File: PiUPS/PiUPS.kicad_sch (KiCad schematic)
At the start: 111 parts, among them J1 USB_C_Receptacle_USB2.0, J2 USB_B_Micro, J3 Screw_Terminal_01x02, J4 Raspberry_Pi_2_3, J5 USB_A, Q1 IRF7404, Q2 IRF7404, Q3 IRLML2803TRPBF, Q4 IRF7404, Q5 IRF7404, Q6 IRLML2803TRPBF, Q7 IRLML2803TRPBF, Q8 IRF7404, Q9 IRLML2803TRPBF, SW1 SW_MEC_5E, SW2 MODE (JS102011SAQN), U1 LM393, U2 BQ25895RTW, U3 DW01, U4 FS8205A, U5 TPS61088RHLR, U6 DS3231M

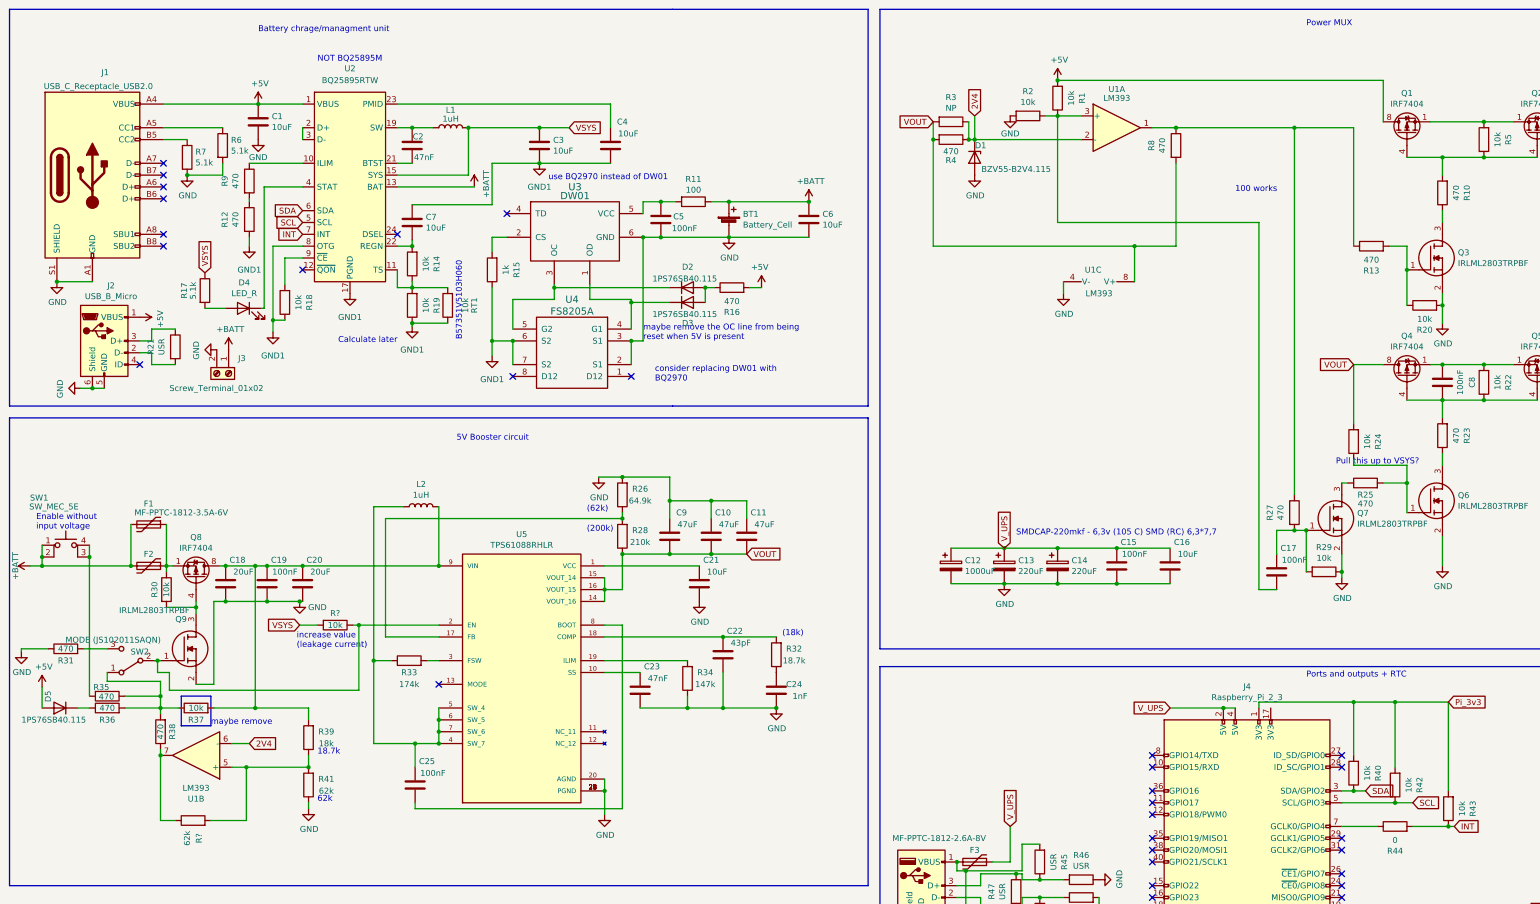
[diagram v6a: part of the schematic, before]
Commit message: updated components and schematic sligtly
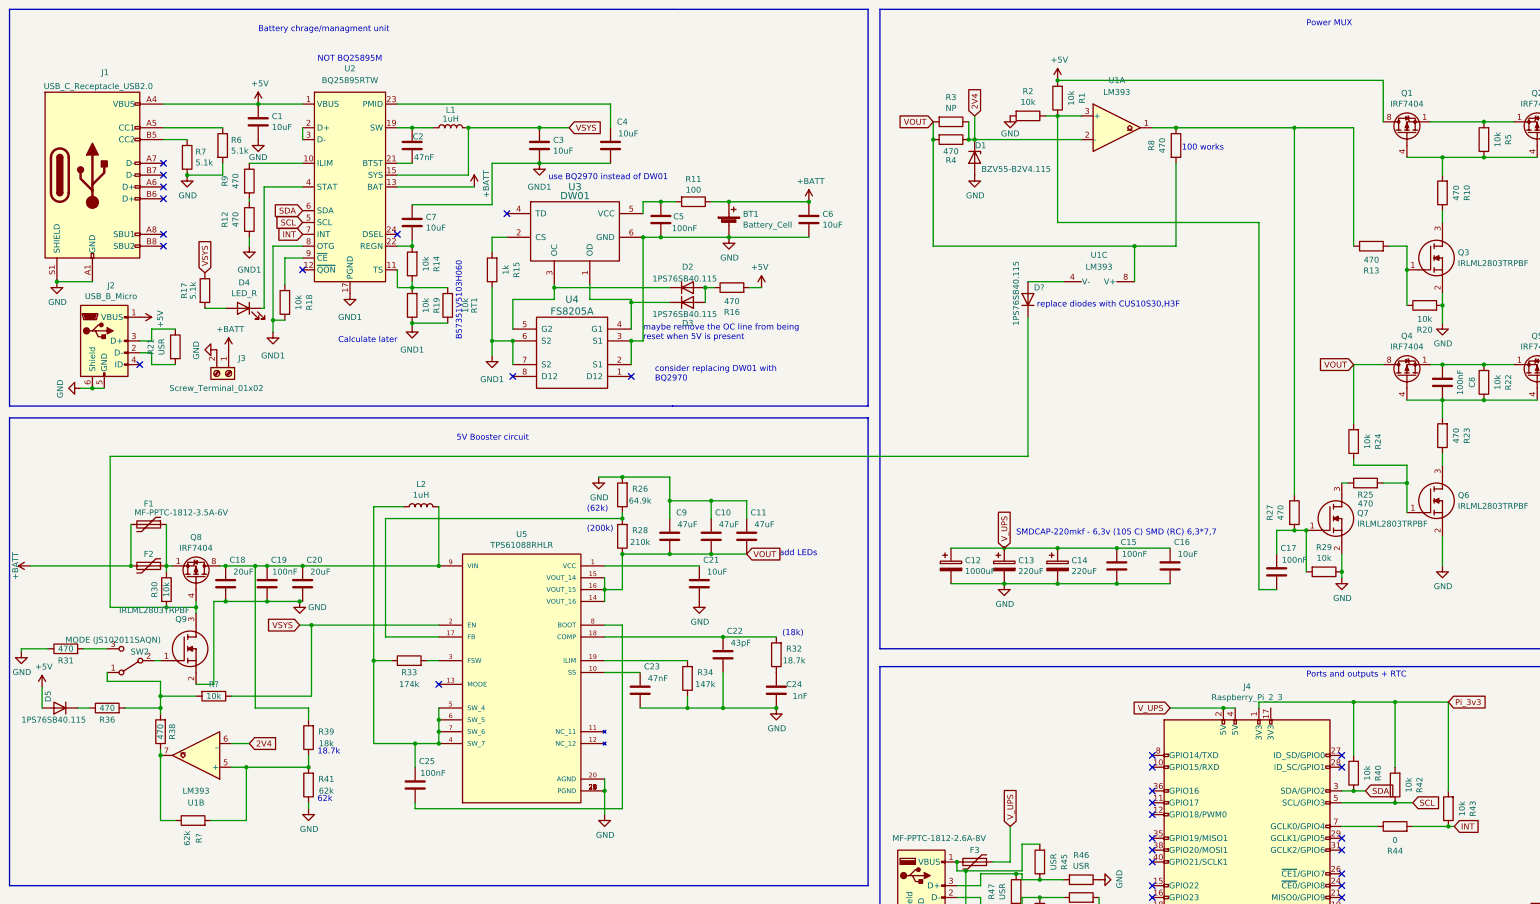
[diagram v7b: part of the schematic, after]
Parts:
- removed R35: 470, Resistor_SMD:R_0805_2012Metric_Pad1.20x1.40mm_HandSolder, symbol Device:R
- removed R37: 10k, Resistor_SMD:R_0805_2012Metric_Pad1.20x1.40mm_HandSolder, symbol Device:R
- removed SW1: SW_MEC_5E, Button_Switch_SMD:SW_SPST_Omron_B3FS-100xP, symbol Switch:SW_MEC_5E
- removed U1: LM393, Package_SO:SOIC-8_3.9x4.9mm_P1.27mm, symbol Amplifier_Operational:LM358
- added D?: 1PS76SB40.115, Diode_SMD:D_SOD-323_HandSoldering, symbol Diode:1N4007
- added U1: LM393, symbol Comparator:LM393
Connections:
- net 2V4: now also U1.2 (-), U1.6 (_)
- net VOUT: now also U1.8 (V+)
- net VSYS: now also R?.1, U5.2 (EN); no longer R?.2
- net at Q9.1, SW2.2 (B): no longer R?.1, U5.2 (EN)
- net at R13.1, R27.1, R8.1: now also U1.1
- net at R36.2, R38.2, SW2.1 (A): now also R?.2
- net at C17.2, R1.1, R2.1: now also U1.3 (+)
- net at R39.1, R41.2, R?.2: now also U1.5 (+)
- net at R38.1, R?.1: now also U1.7
- net at Q8.4 (G), Q9.3, R30.2: now also D?.1 (K)
- new net: D?.2 (A), U1.4 (V-)
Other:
- note added: "add LEDs"
- note added: "replace diodes with CUS10S30,H3F"
- note removed: "Enable without input voltage"
- note removed: "Pull this up to VSYS?"
- note removed: "increase value (leakage current)"
- note removed: "maybe remove"
- moved on the sheet: R?

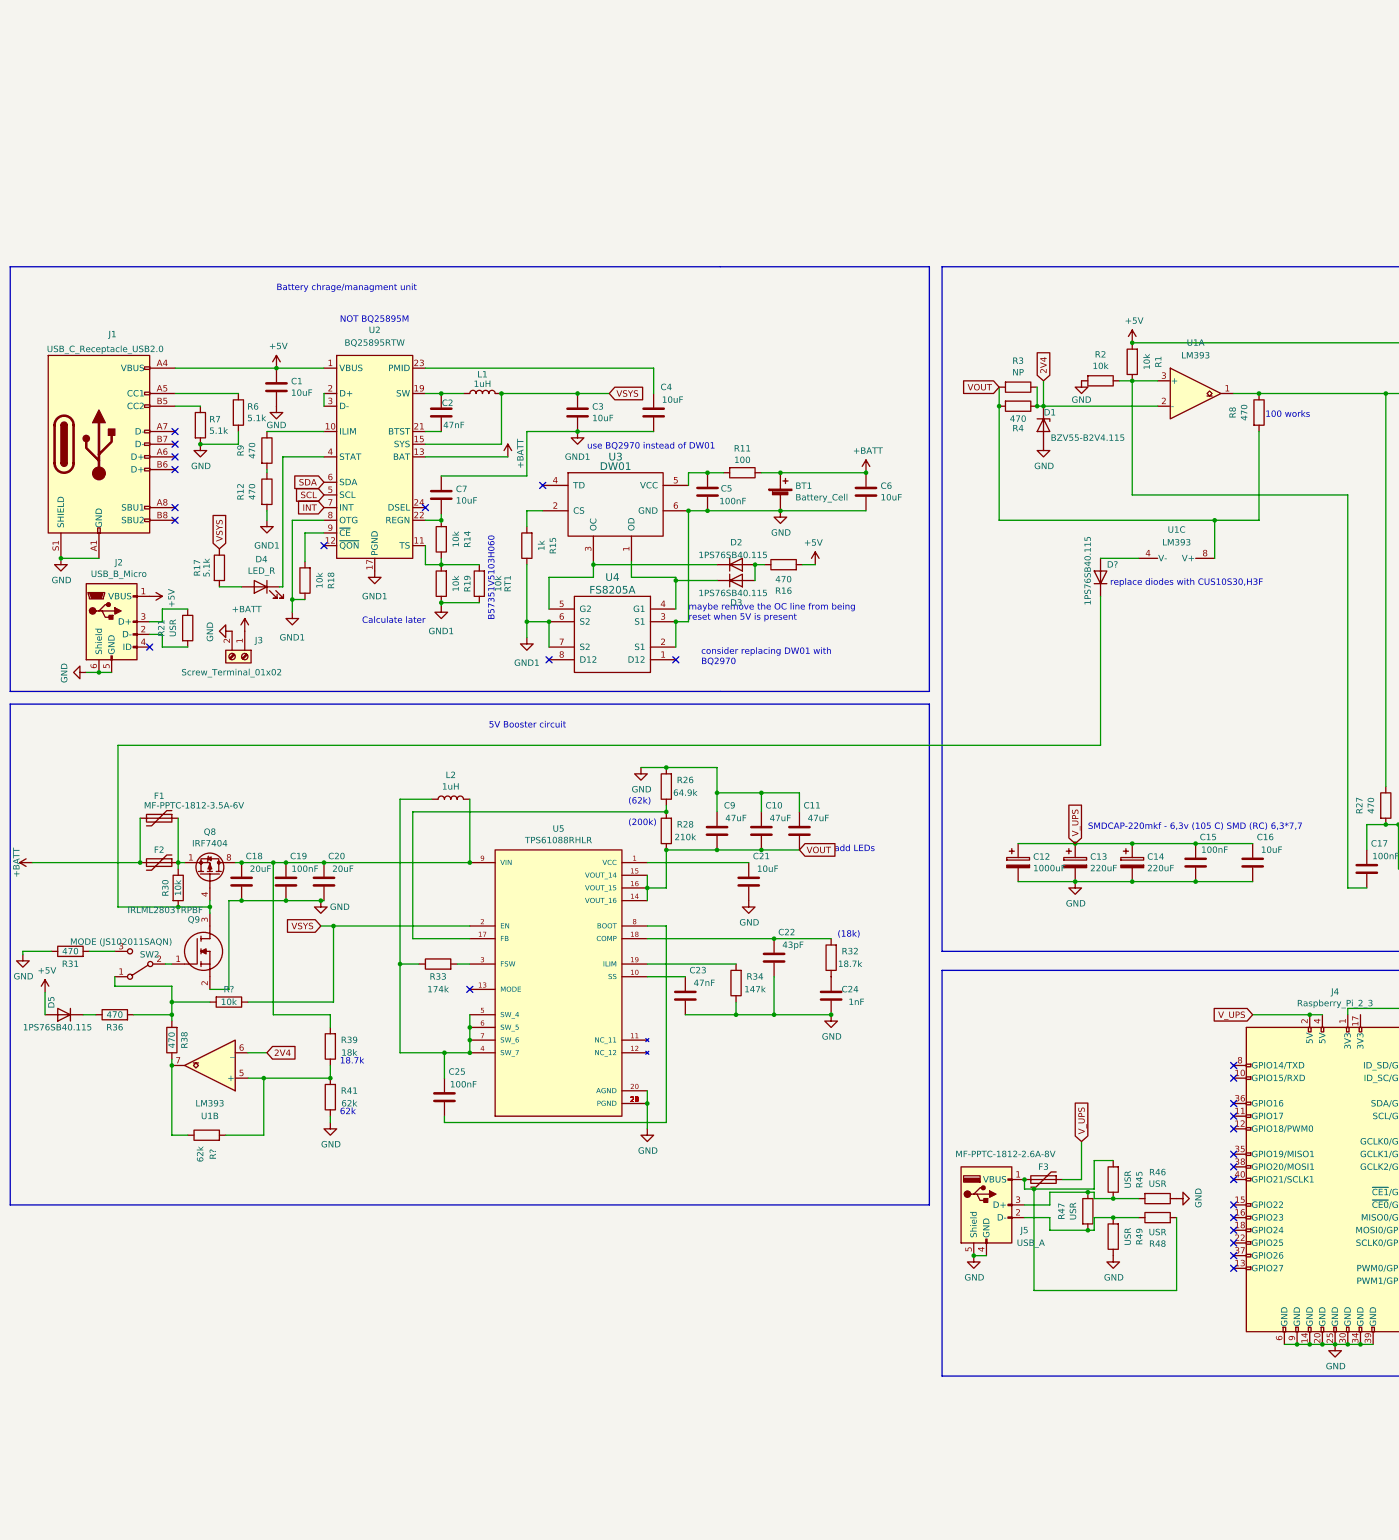
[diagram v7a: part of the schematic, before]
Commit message: updated shcematic with new battery protection system and some notes
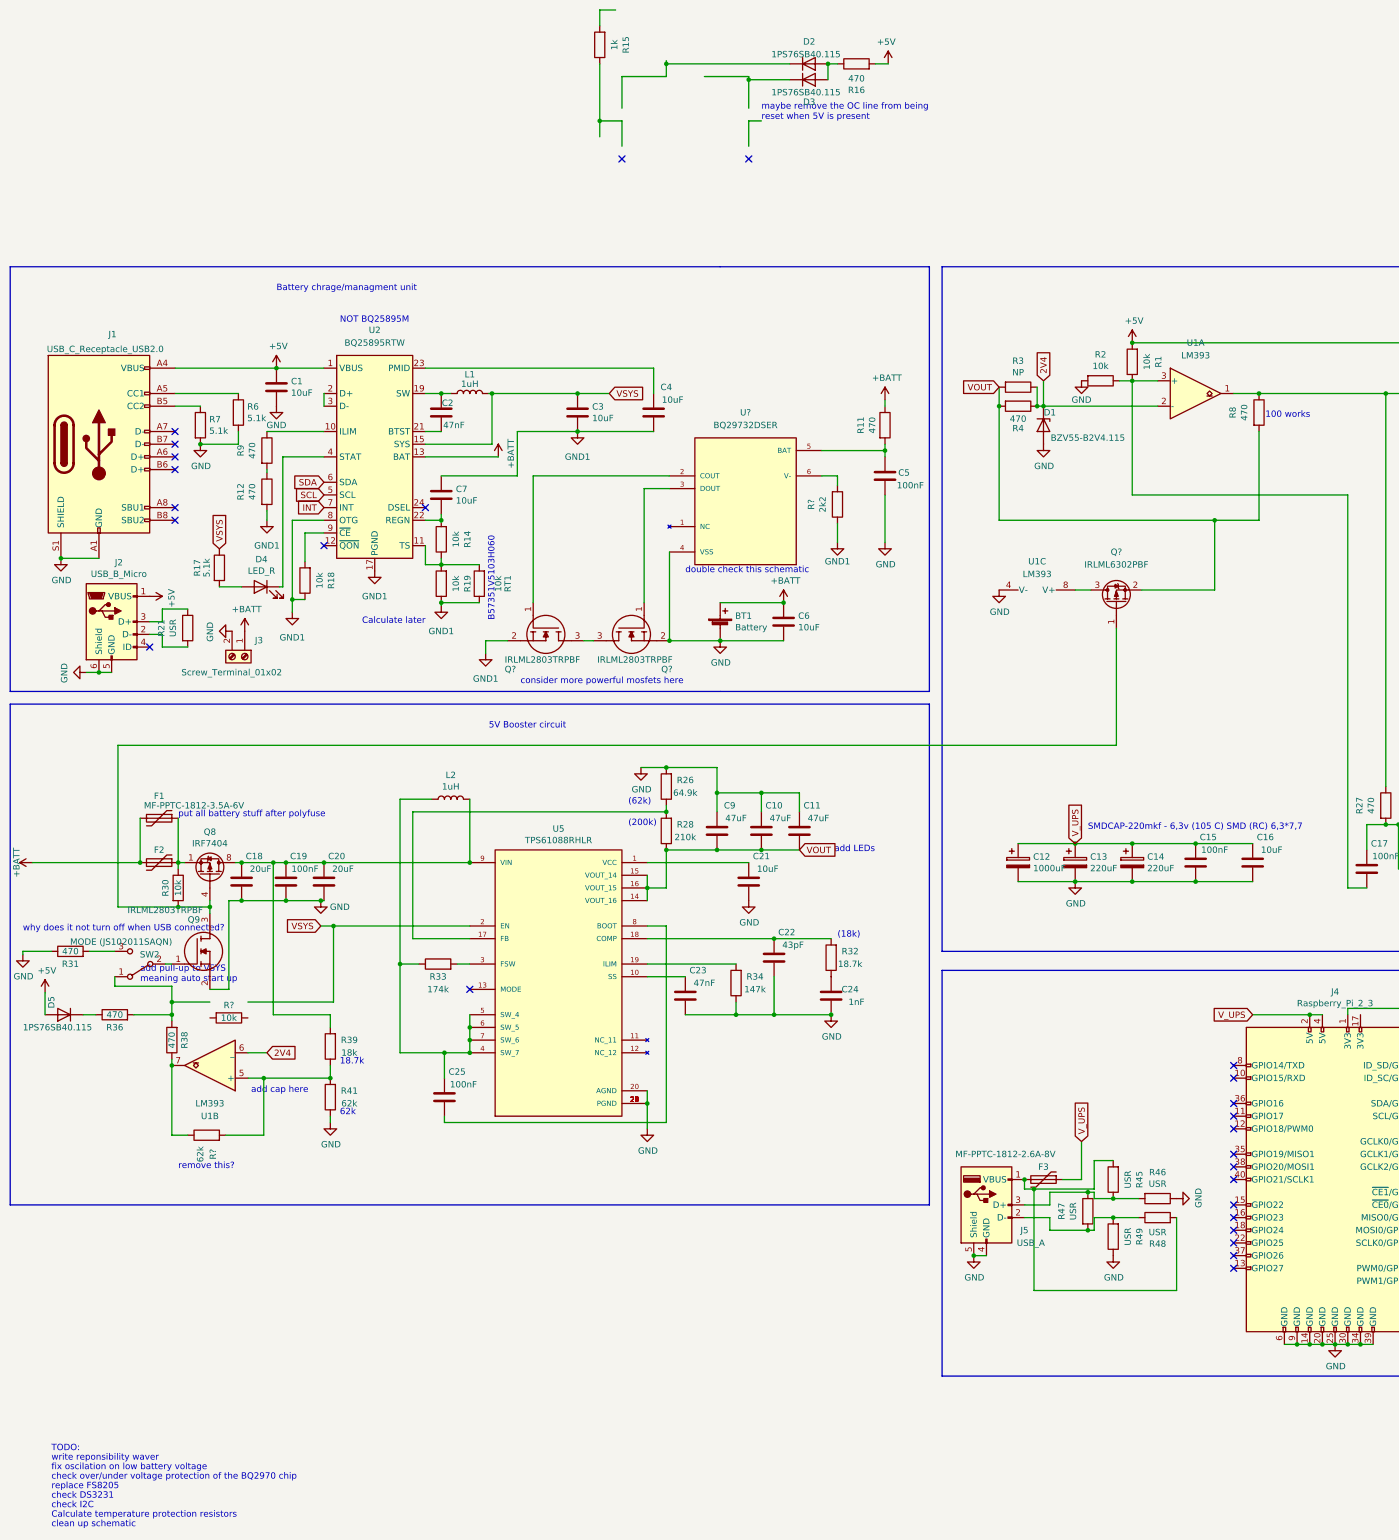
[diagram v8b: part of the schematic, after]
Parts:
- removed D?: 1PS76SB40.115, Diode_SMD:D_SOD-323_HandSoldering, symbol Diode:1N4007
- removed U3: DW01, Package_TO_SOT_SMD:SOT-23-6, symbol dw01:DW01
- removed U4: FS8205A, Package_SO:TSSOP-8_4.4x3mm_P0.65mm, symbol fs8205a:FS8205A
- added Q? (x2): IRLML2803TRPBF, IRLML2803TRPBF:SOT95P237X112-3N, symbol IRLML2803TRPBF:IRLML2803TRPBF
- added Q?: IRLML6302PBF, symbol Device:Q_PMOS_GSD
- added R?: 2k2, Resistor_SMD:R_0805_2012Metric_Pad1.20x1.40mm_HandSolder, symbol Device:R
- added U?: BQ29732DSER, SON50P150X150X80-6N, symbol BQ29700DSER:BQ29700DSER
- BT1: value Battery_Cell -> Battery
- R11: value 100 -> 470
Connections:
- net GND: now also U1.4 (V-), Q?.2, U?.4 (VSS)
- net GND1: now also Q?.2, R?.1; no longer R15.1
- net VOUT: now also Q?.2 (S); no longer U1.8 (V+)
- net VSYS: no longer R?.1
- net at R36.2, R38.2, SW2.1 (A): no longer R?.2
- net at Q8.4 (G), Q9.3, R30.2: now also Q?.1 (G)
- net at C5.1, R11.2: now also U?.5 (BAT)
- new net: Q?.1, U?.2 (COUT)
- new net: Q?.3, Q?.3
- new net: Q?.3 (D), U1.8 (V+)
- new net: Q?.1, U?.3 (DOUT)
- new net: R?.2, U?.6 (V-)
- no-connect marks 41 -> 40
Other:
- note added: "Calculate temperature protection resistors"
- note added: "TODO:"
- note added: "add cap here"
- note added: "add pull-up to VSYS meaning auto start up"
- note added: "check DS3231"
- note added: "check I2C"
- note added: "check over/under voltage protection of the BQ2970 chip"
- note added: "clean up schematic"
- note added: "consider more powerful mosfets here"
- note added: "double check this schematic"
- note added: "fix oscilation on low battery voltage"
- note added: "put all battery stuff after polyfuse"
- note added: "remove this?"
- note added: "replace FS8205"
- note added: "why does it not turn off when USB connected?"
- note added: "write reponsibility waver"
- note removed: "consider replacing DW01 with BQ2970"
- note removed: "replace diodes with CUS10S30,H3F"
- note removed: "use BQ2970 instead of DW01"
- moved on the sheet: BT1, C5, C6, D2, D3, L1, R11, R15, R16, R?, U1C
